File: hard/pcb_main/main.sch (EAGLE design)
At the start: 209 parts

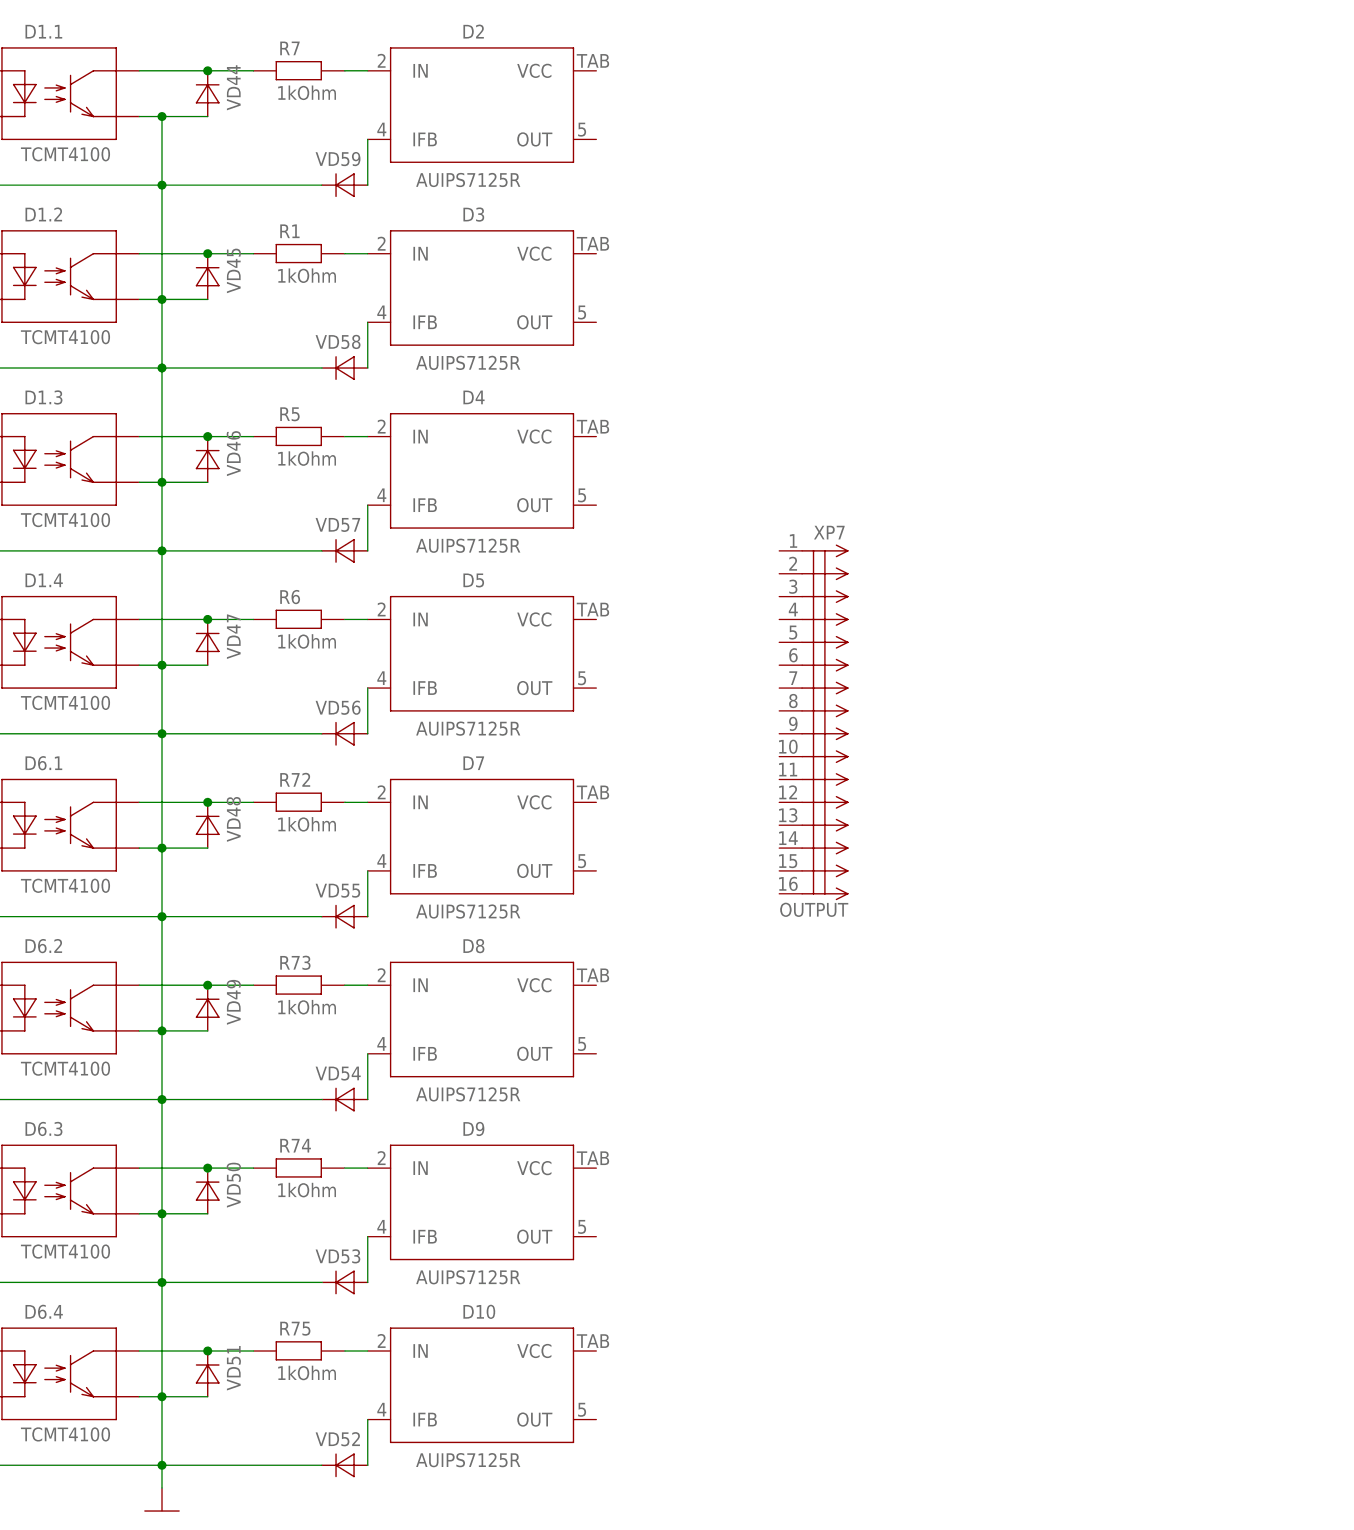
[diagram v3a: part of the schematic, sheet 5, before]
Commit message: power supply routed
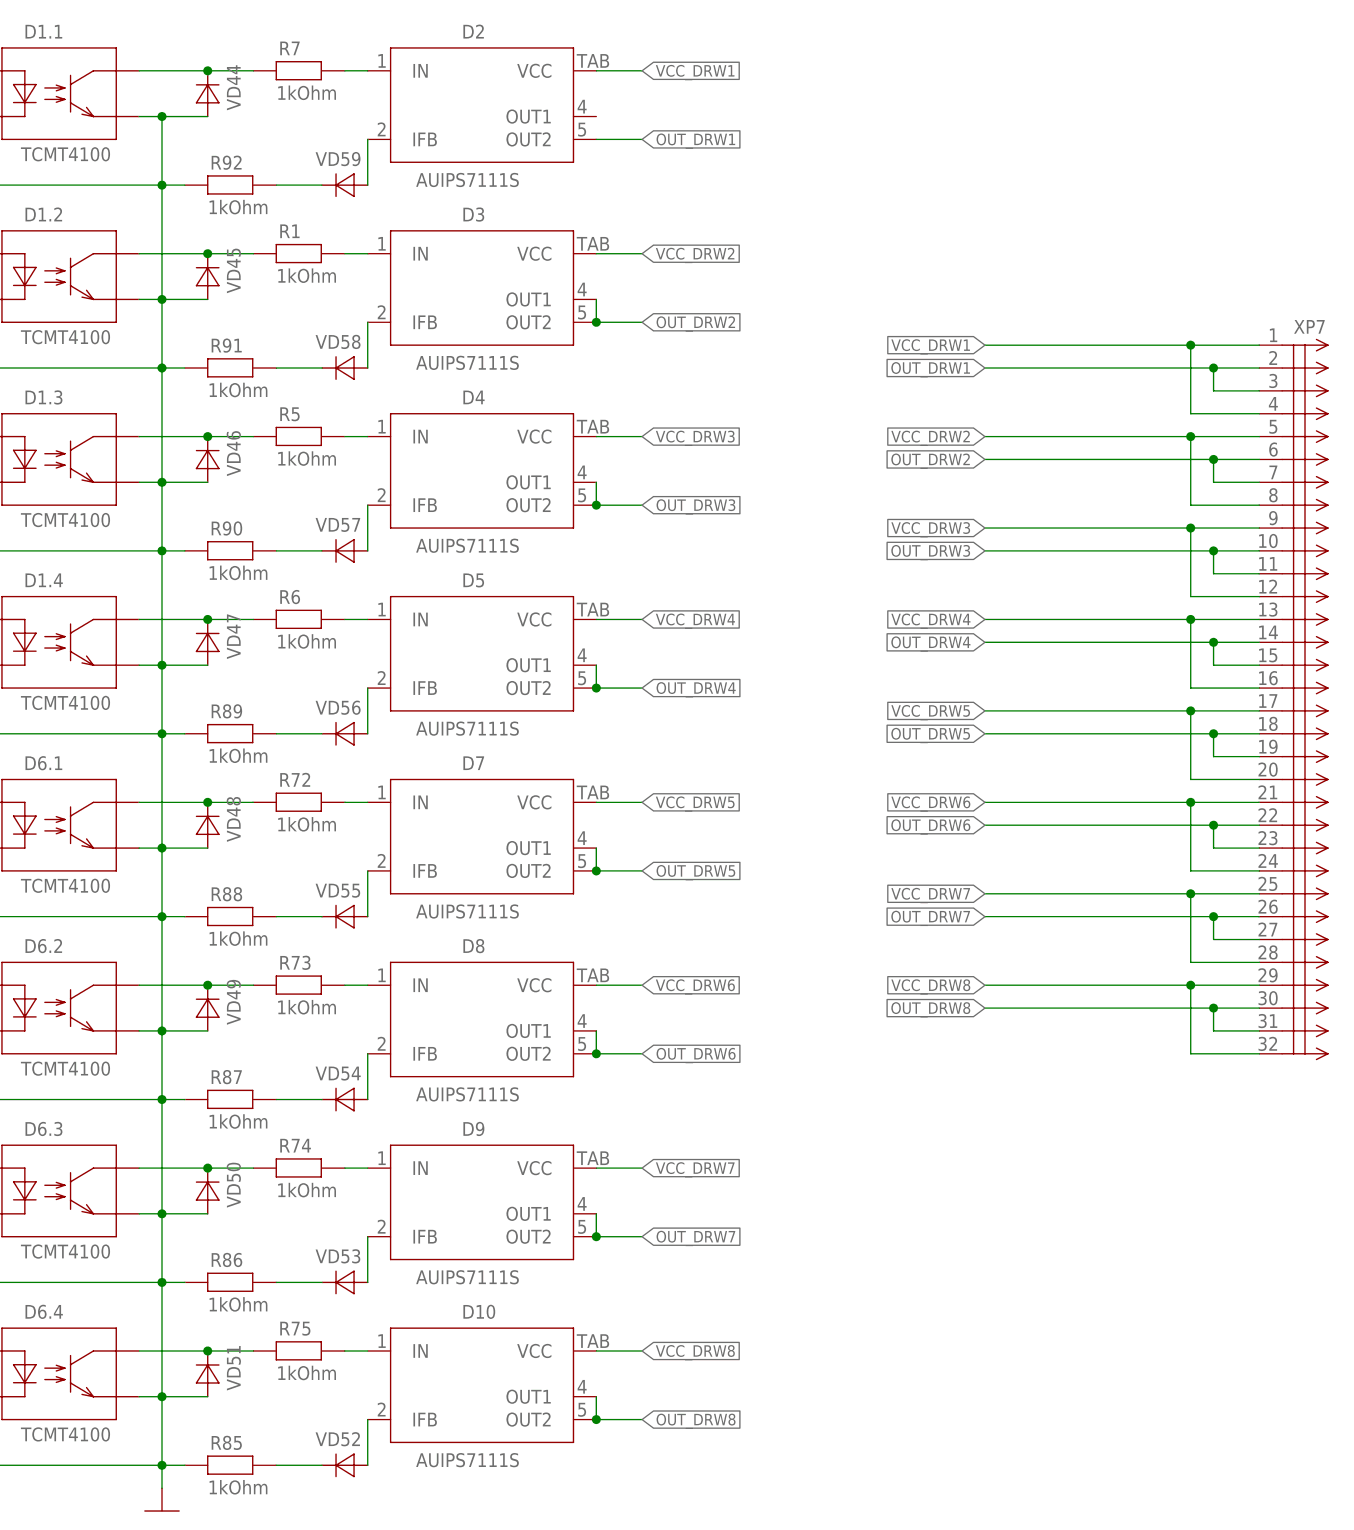
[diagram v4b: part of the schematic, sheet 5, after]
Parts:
- added C30, C31: 10uF/50V, rcl:C-EUC2220K
- added C32, C33: 0.1uF, rcl:C-EUC0603
- added R85, R86, R87, R88, R89, R90, R91, R92: 1kOhm, rcl:R-EU_R0805
- added RK1: 0.5A, fuse:RESETTABLE_FUSE_1210
- added RK2: 2A, fuse:RESETTABLE_FUSE_1812
- C1, C3: value 220uF/10v -> 220uF/10V
- D10, D2, D3, D4, D5, D7, D8, D9: value AUIPS7125R -> AUIPS7111S; device transistor-fet:AUIPS7125R -> transistor-fet:AUIPS7111S; PARTNO AUIPS7125RTRL -> AUIPS7111S
- L1: value 33uH -> 47uH; PARTNO DR125-470-R -> DR127-470-R
- L2: value 33uH -> 100uH; device inductor-cooper:DRA127 -> inductor-cooper:DRA73; PARTNO DR125-470-R -> DR73-101-R
- VD1: value (none) -> 3A/60V; PARTNO VS-30BQ040PBF -> VS-30BQ060TRPBF
- VD2: value (none) -> 1A/60V; device diode:DIODE-SCHOTTKY-SMC -> diode:DIODE-SCHOTTKY-SMB; PARTNO VS-30BQ040PBF -> VS-10BQ060TRPBF
- XP7: value OUTPUT -> (none); device connector:TYCO-174053(2.54) -> connector:PLD_2X16; PARTNO * -> (none)
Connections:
- new net N$75: R92.2, VD59.C
- new net N$76: R91.2, VD58.C
- new net N$77: R90.2, VD57.C
- new net N$78: R89.2, VD56.C
- new net N$79: R88.2, VD55.C
- new net N$82: R87.2, VD54.C
- new net N$83: R86.2, VD53.C
- new net N$84: R85.2, VD52.C
- new net N$85: C1.+, DA1.FB, L1.2, RK2.P$1
- new net N$86: C3.-, DA2.!ON!/OFF, DA2.GND, DA2.GND@6, RK1.P$1, VD2.A
- new net OUT_DRW1: D2.OUT2, XP7.2, XP7.3
- new net OUT_DRW2: D3.OUT1, D3.OUT2, XP7.6, XP7.7
- new net OUT_DRW3: D4.OUT1, D4.OUT2, XP7.10, XP7.11
- new net OUT_DRW4: D5.OUT1, D5.OUT2, XP7.14, XP7.15
- new net OUT_DRW5: D7.OUT1, D7.OUT2, XP7.18, XP7.19
- new net OUT_DRW6: D8.OUT1, D8.OUT2, XP7.22, XP7.23
- new net OUT_DRW7: D9.OUT1, D9.OUT2, XP7.26, XP7.27
- new net OUT_DRW8: D10.OUT1, D10.OUT2, XP7.30, XP7.31
- new net VCC_DRW1: D2.VCC, XP7.1, XP7.4
- new net VCC_DRW2: D3.VCC, XP7.5, XP7.8
- new net VCC_DRW3: D4.VCC, XP7.12, XP7.9
- new net VCC_DRW4: D5.VCC, XP7.13, XP7.16
- new net VCC_DRW5: D7.VCC, XP7.17, XP7.20
- new net VCC_DRW6: D8.VCC, XP7.21, XP7.24
- new net VCC_DRW7: D9.VCC, XP7.25, XP7.28
- new net VCC_DRW8: D10.VCC, XP7.29, XP7.32
- net +24V: now also XP9.5, XP9.7; no longer XP9.2, XP9.4
- net +24V_CLEAR: now also C30.1, C31.2, C32.1, C33.2
- net +5V: now also RK2.P$2; no longer C3.+, DA1.FB, L1.2
- net -5V: now also RK1.P$2; no longer C1.-, DA2.!ON!/OFF, DA2.GND, DA2.GND@6, VD2.A
- net GND: now also C1.-, C3.+, C30.2, C31.1, C32.2, C33.1, R85.1, R86.1, R87.1, R88.1, R89.1, R90.1, R91.1, R92.1, XP9.2, XP9.4; no longer C1.+, C3.-, VD52.C, VD53.C, VD54.C, VD55.C, VD56.C, VD57.C, VD58.C, VD59.C, XP9.5, XP9.7
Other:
- note removed: "fuse 0.5A"
- note removed: "fuse 2A"
- moved on the sheet: C1, C2, C3, DA2, L1, L2, VD1, VD2, VD26

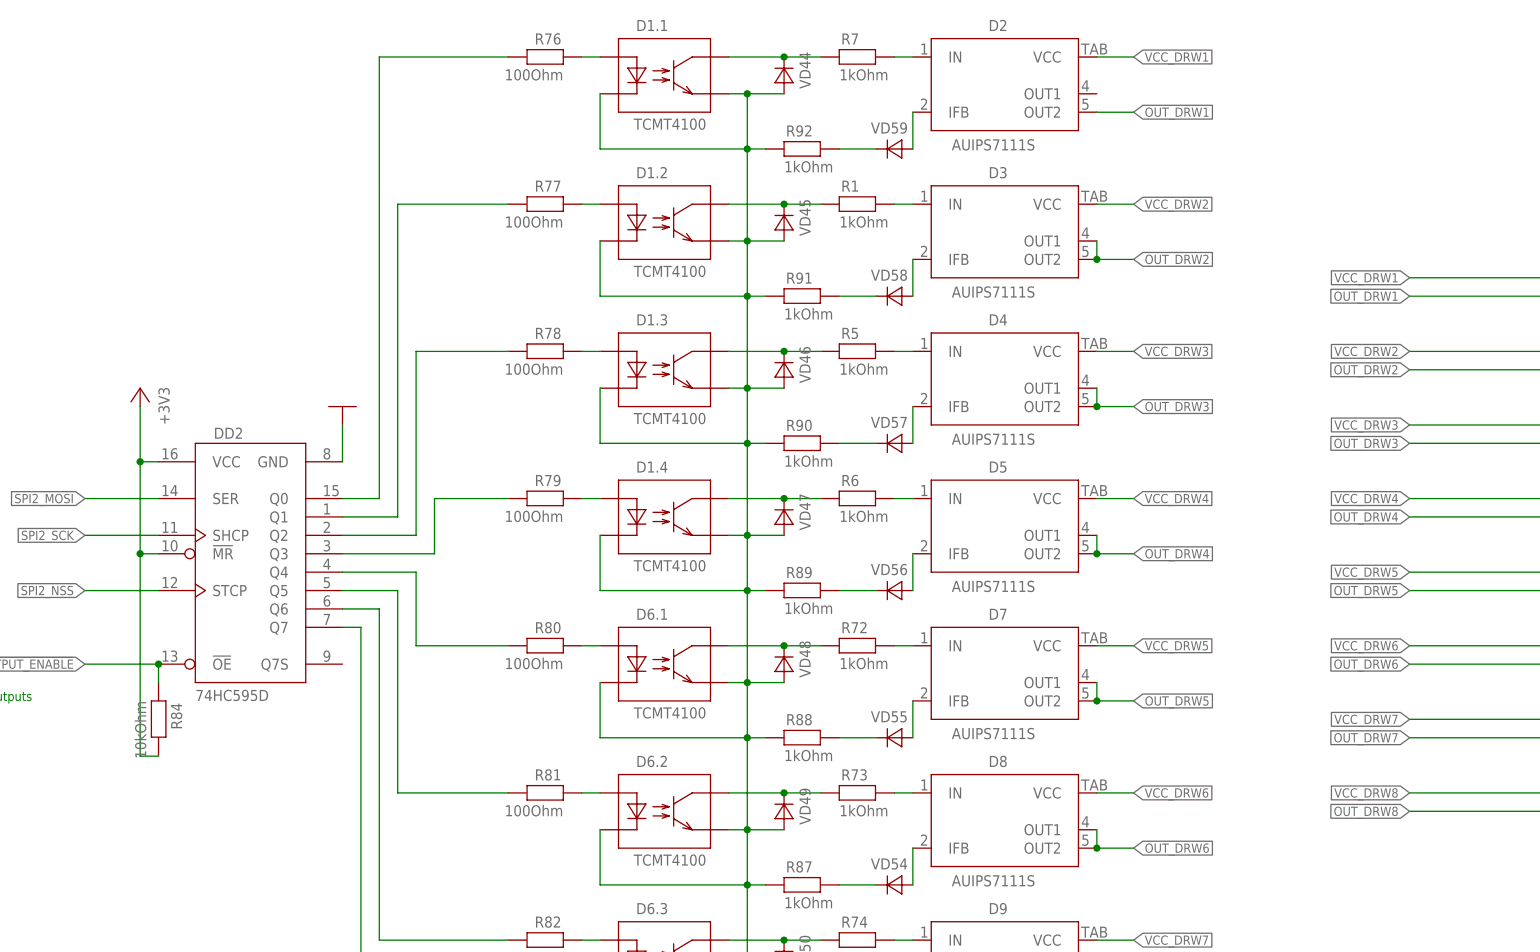
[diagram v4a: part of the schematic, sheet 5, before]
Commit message: outputs routed
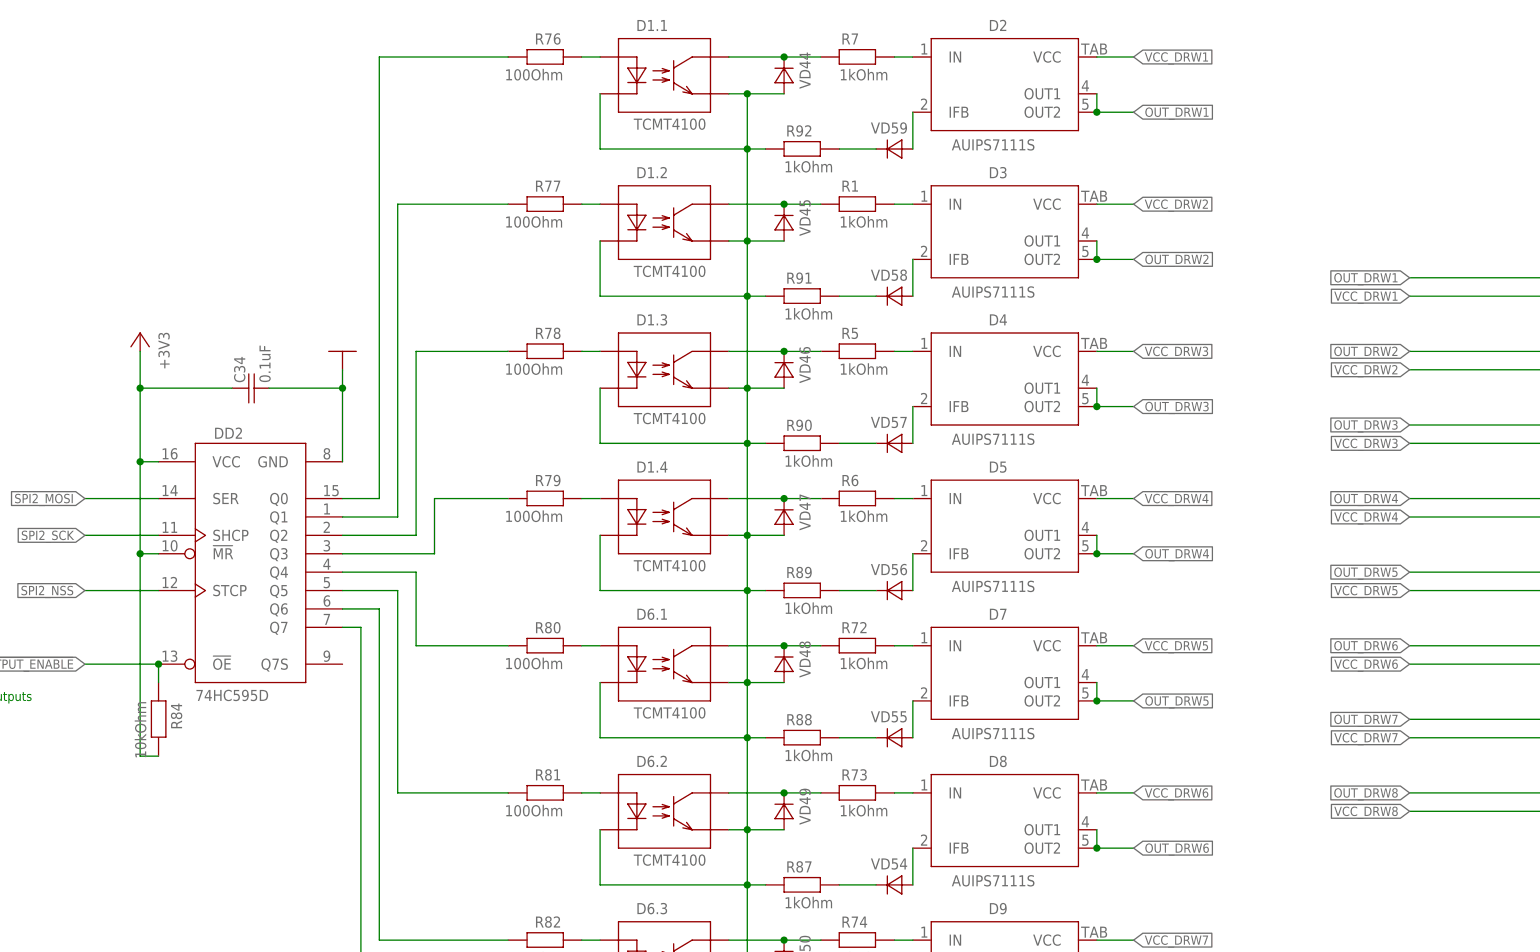
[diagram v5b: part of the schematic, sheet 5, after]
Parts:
- added C34: 0.1uF, rcl:C-EUC0603
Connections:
- net +3V3: now also C34.1
- net GND: now also C34.2
- net OUT_DRW1: now also D2.OUT1, XP7.1, XP7.4; no longer XP7.2, XP7.3
- net OUT_DRW2: now also XP7.5, XP7.8; no longer XP7.6, XP7.7
- net OUT_DRW3: now also XP7.12, XP7.9; no longer XP7.10, XP7.11
- net OUT_DRW4: now also XP7.13, XP7.16; no longer XP7.14, XP7.15
- net OUT_DRW5: now also XP7.17, XP7.20; no longer XP7.18, XP7.19
- net OUT_DRW6: now also XP7.21, XP7.24; no longer XP7.22, XP7.23
- net OUT_DRW7: now also XP7.25, XP7.28; no longer XP7.26, XP7.27
- net OUT_DRW8: now also XP7.29, XP7.32; no longer XP7.30, XP7.31
- net VCC_DRW1: now also XP7.2, XP7.3; no longer XP7.1, XP7.4
- net VCC_DRW2: now also XP7.6, XP7.7; no longer XP7.5, XP7.8
- net VCC_DRW3: now also XP7.10, XP7.11; no longer XP7.12, XP7.9
- net VCC_DRW4: now also XP7.14, XP7.15; no longer XP7.13, XP7.16
- net VCC_DRW5: now also XP7.18, XP7.19; no longer XP7.17, XP7.20
- net VCC_DRW6: now also XP7.22, XP7.23; no longer XP7.21, XP7.24
- net VCC_DRW7: now also XP7.26, XP7.27; no longer XP7.25, XP7.28
- net VCC_DRW8: now also XP7.30, XP7.31; no longer XP7.29, XP7.32
